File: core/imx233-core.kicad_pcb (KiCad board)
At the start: 4 copper layers, 48.3 x 48.3 mm, 61 parts, among them J1 Conn_01x15, J2 Conn_01x19, J3 Conn_01x19, J4 Conn_01x02, J5 USB_B_Micro, U1 MCIMX233CAG4C, U2 MT46V32M16, X1 24MHz

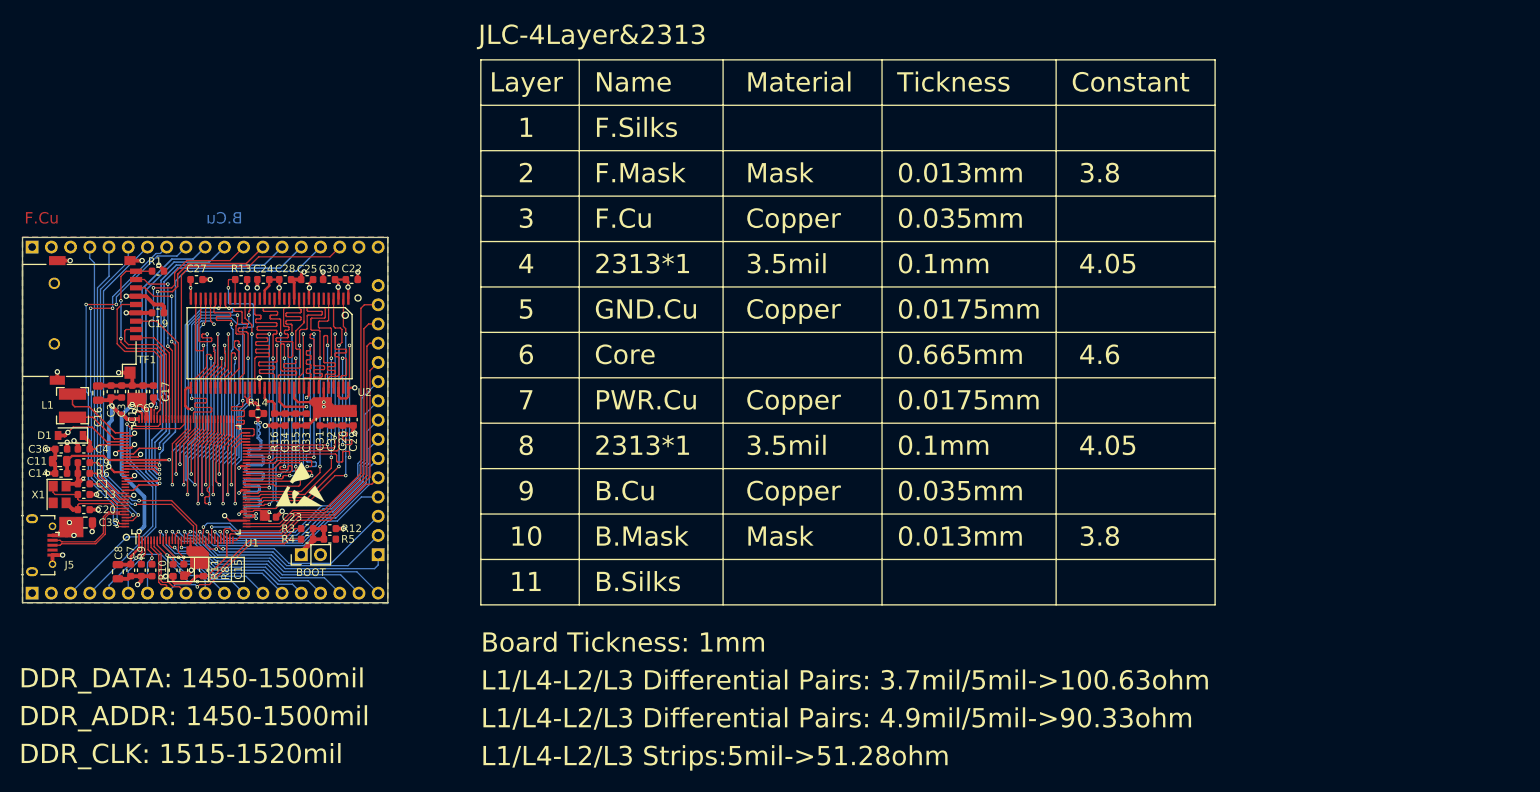
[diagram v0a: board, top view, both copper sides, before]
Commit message: core: Add ESD protection to USB
Update mx233 symbol & footprint library.
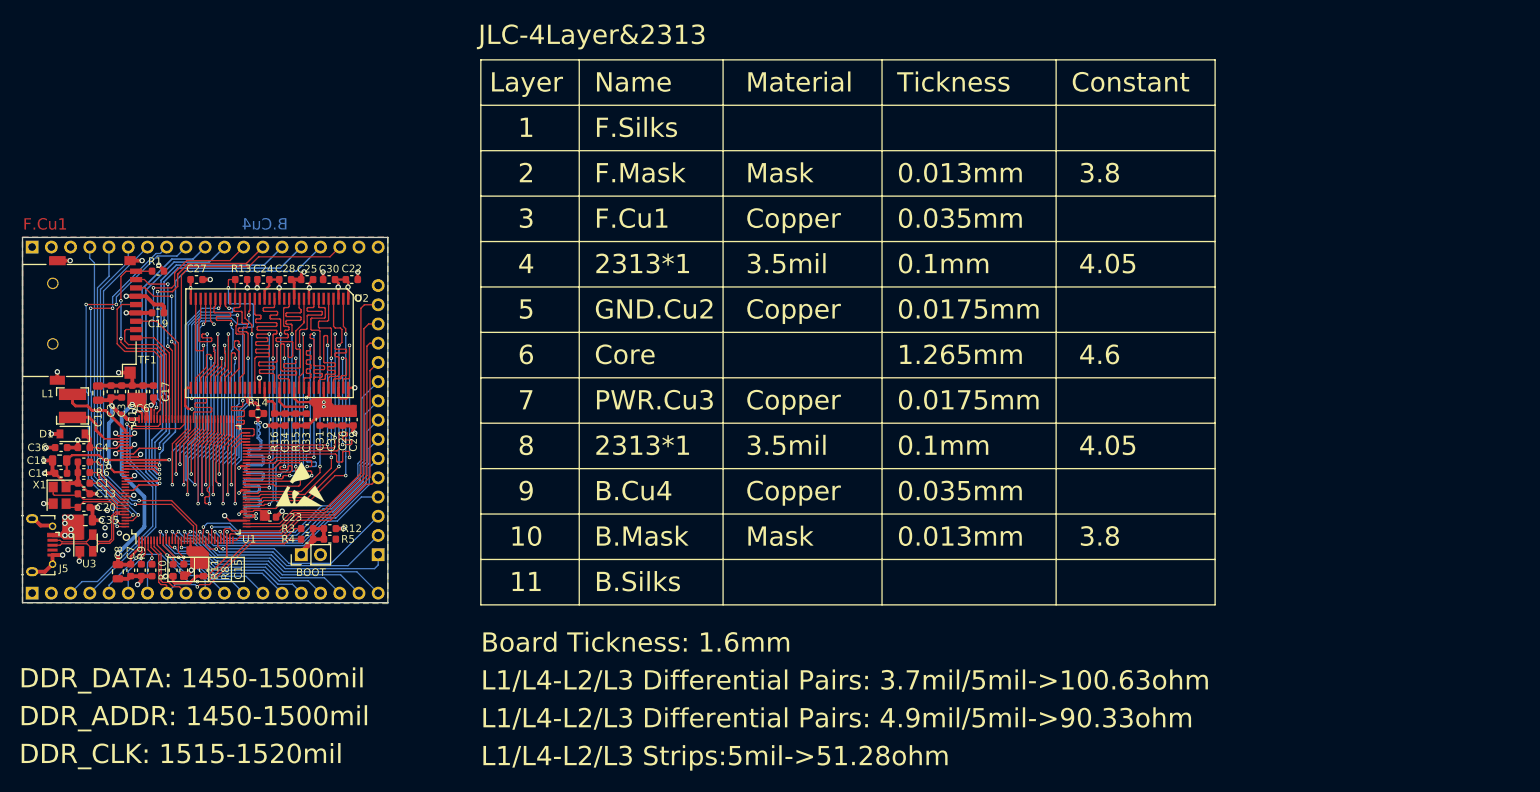
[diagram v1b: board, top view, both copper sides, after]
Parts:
- added U3: SR05, Package_TO_SOT_SMD:SOT-143, F.Cu at (80.4, 124.4)
- J5: footprint Lib:USB_Micro-Molex -> Library:USB_Micro-Molex
- L1: footprint Lib:Inductor-4x4 -> Library:Inductor-4x4
- TF1: footprint Lib:XKXFS-N02-XXT -> Library:XKXFS-N02-XXT
- U1: footprint Lib:LQFP-128_14x14_Pitch0.4mm -> Library:LQFP-128_14x14_Pitch0.4mm
- U2: footprint Lib:TSSOP-66_400mil_P0.65mm -> Library:TSSOP-66_400mil_P0.65mm
- X1: footprint Lib:Crystal_SMD_3225-4P_3.2x2.5mm -> Library:Crystal_SMD_3225-4P_3.2x2.5mm
- moved REF** 19.8 mm to (81.6, 115.3)
- moved G*** 9.32 mm to (81.6, 100.3)
- moved REF** 4.80 mm to (102.1, 116.8)
- moved D1 0.32 mm to (78.7, 110.0)
- moved C35 0.30 mm to (80.4, 121.4)
- moved C20 0.30 mm to (80.2, 119.7)
- moved C36 0.20 mm to (77.2, 111.8), turned to 180 degrees
- moved C4 0.20 mm to (80.2, 111.8)
- moved X1 0.11 mm to (77.0, 118.1)
- moved C13 0.10 mm to (80.2, 117.9)
- moved R6 0.10 mm to (80.2, 115.1)
- moved C1 0.10 mm to (80.2, 116.5)
- moved C11 0.10 mm to (77.0, 113.5)
- moved C9 0.10 mm to (80.2, 113.7)
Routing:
- net GND: track 106.4 -> 122.0 mm, vias 34 -> 42
- net +BATT: track 11.6 -> 4.01 mm, vias 2 -> 3
- net +5V: track 8.23 -> 12.6 mm, vias 4 -> 8
- net +1V2: track 31.2 -> 35.5 mm
- net /USBD_P: track 12.7 -> 14.2 mm
- net /USBD_N: track 12.7 -> 13.9 mm
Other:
- board text added: "1.265mm"
- board text added: "B.Cu4"
- board text added: "Board Tickness: 1.6mm"
- board text added: "F.Cu1"
- board text added: "GND.Cu2"
- board text added: "Layout 2020-08-23"
- board text added: "Licensed under the"
- board text added: "Openboard V6.12"
- board text added: "PWR.Cu3"
- board text added: "TAPR Open Hardware License (www.tapr.org/OHL)"
- board text added: "bbs.xboard.io"
- board text removed: "0.665mm"
- board text removed: "B.Cu"
- board text removed: "Board Tickness: 1mm"
- board text removed: "F.Cu"
- board text removed: "GND.Cu"
- board text removed: "Layout 2020-06-11"
- board text removed: "OpenBoard V6.11"
- board text removed: "PWR.Cu"
